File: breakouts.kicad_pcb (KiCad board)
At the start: 2 copper layers, 100 x 92.6 mm, 211 parts, among them IC901 ATTINY85-S, J1101 USB_MINI-B, J1201 JACK_5P, J201 USB_MINI-B, J301 USB_MINI-B, J401 SMA, J801 USB_MINI-B, K1201 CONN_3, K1301 CONN_3, K601 CONN_3, K801 CONN_3, P1001 CONN_4, P1002 CONN_4, P1101 CONN_6, P1102 CONN_6, P1201 CONN_2, P1202 CONN_2, P1203 CONN_2, P1301 CONN_2, P201 CONN_2, P202 CONN_2, P203 CONN_2, P301 CONN_6, P302 CONN_6, P401 CONN_8, P402 CONN_8, P501 CONN_2, P502 CONN_2, P701 POWER, P702 PORT B, P703 PORT C, P704 PORT D, P705 ISP, P801 PORT B, P802 PORT C, P803 PORT D, P804 ISP, P901 CONN_8, P902 ISP, SW701 SW_PUSH, SW801 SW_PUSH, SW901 SW_PUSH, U1001 SST25VF016B, U1101 FT230X-QFN, U1201 TDA1517ATW, U1301 MCP7940M, U301 FT230X, U401 MRF49XA, U501 SP6641A/B, U601 NX1117C33Z, U701 ATMEGA88PA-A, U801 ATMEGA32U2, X1301 32.768kHz, X401 10MHz, X701 12MHz 18pF, X801 16MHz 18pF

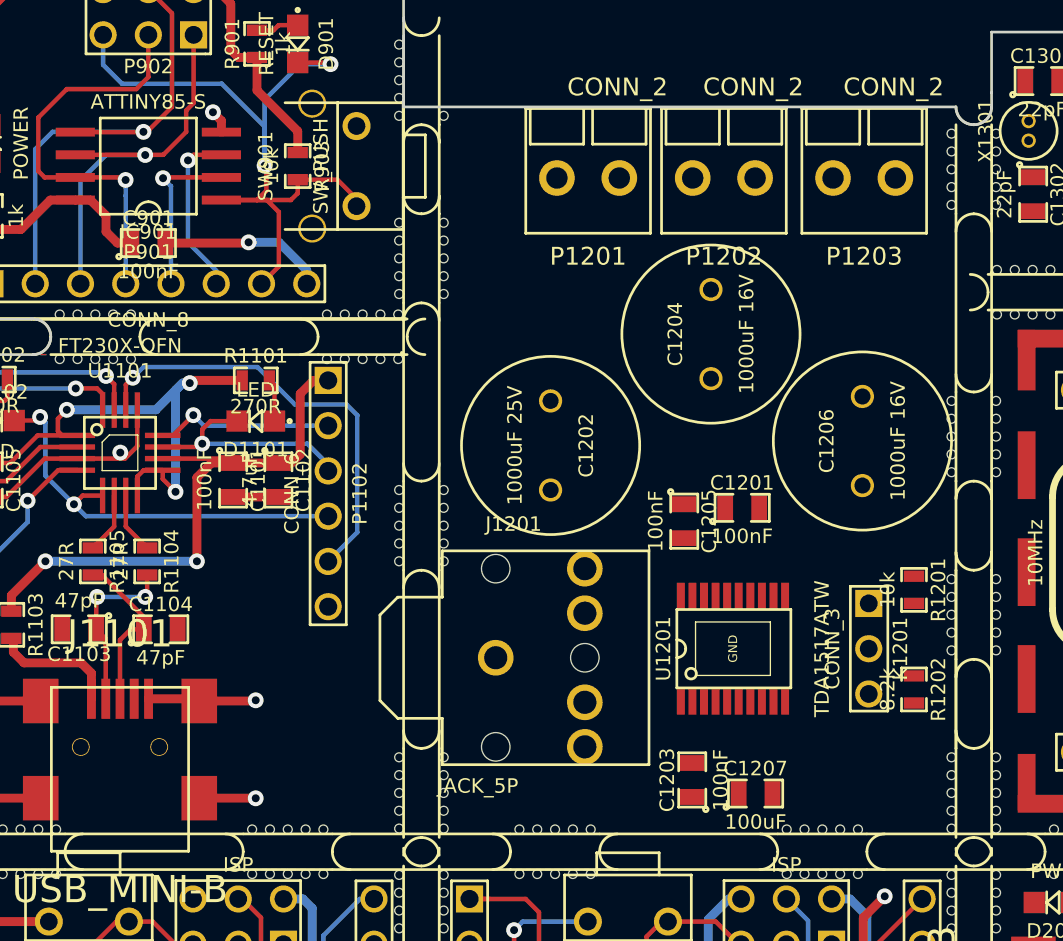
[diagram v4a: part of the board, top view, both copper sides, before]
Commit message: Route Audio amplifier board
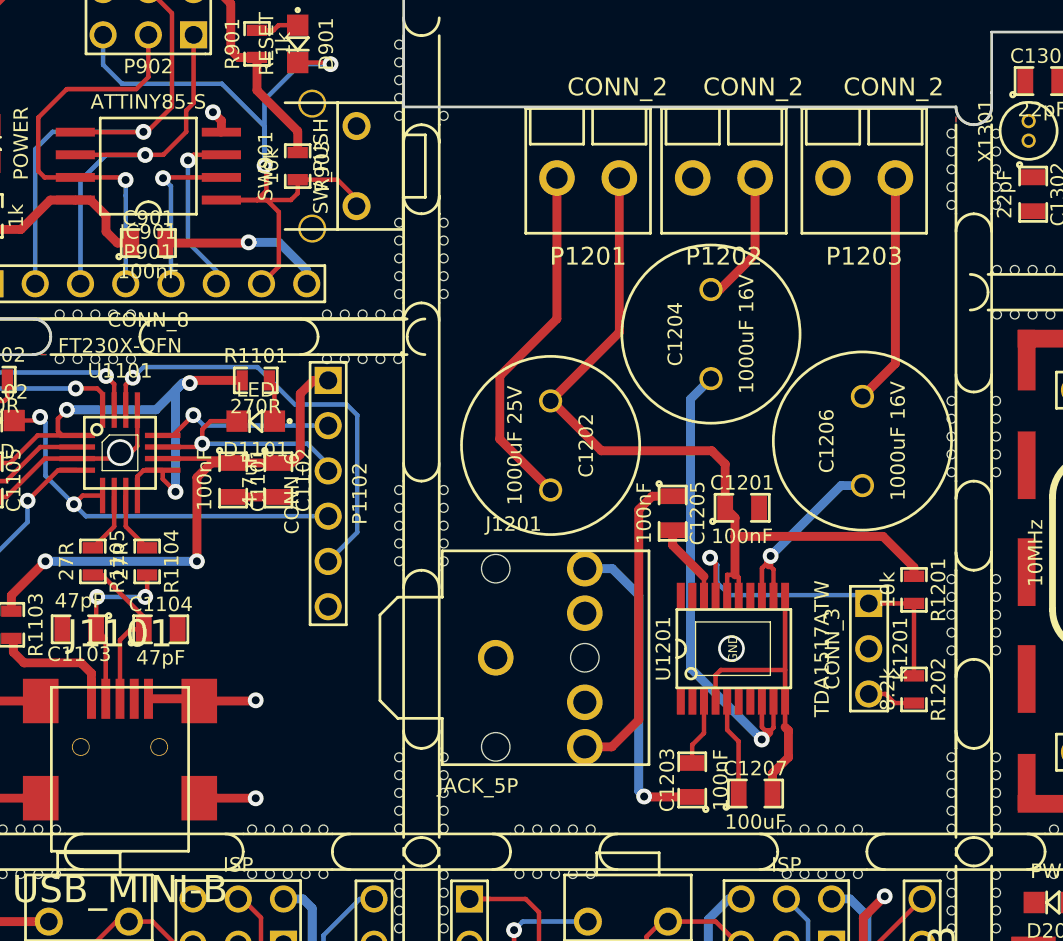
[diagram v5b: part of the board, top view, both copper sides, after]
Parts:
- moved C1205 0.79 mm to (70.1, 86.3)
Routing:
- net VCC11: track 0.00 -> 46.0 mm
- net GND11: track 0.00 -> 37.0 mm
- net N-00000168: track 0.00 -> 27.0 mm, vias 0 -> 1
- net /Audio amplifier/StandBy: track 0.00 -> 19.4 mm, vias 0 -> 1
- net N-00000161: track 0.00 -> 17.8 mm, vias 0 -> 1
- net N-00000162: track 0.00 -> 17.7 mm
- net N-00000170: track 0.00 -> 13.0 mm
- net N-00000166: track 0.00 -> 11.3 mm, vias 0 -> 1
- net N-00000169: track 0.00 -> 7.58 mm
- net N-00000158: track 0.00 -> 5.44 mm
- net N-00000160: track 0.00 -> 4.43 mm
- net N-00000159: track 0.00 -> 3.74 mm
- net /Audio amplifier/Mute: track 0.00 -> 2.75 mm
- net (no net): vias 2 -> 3
- added copper zone on B.Cu, net GND11
- added copper zone on F.Cu, net GND11

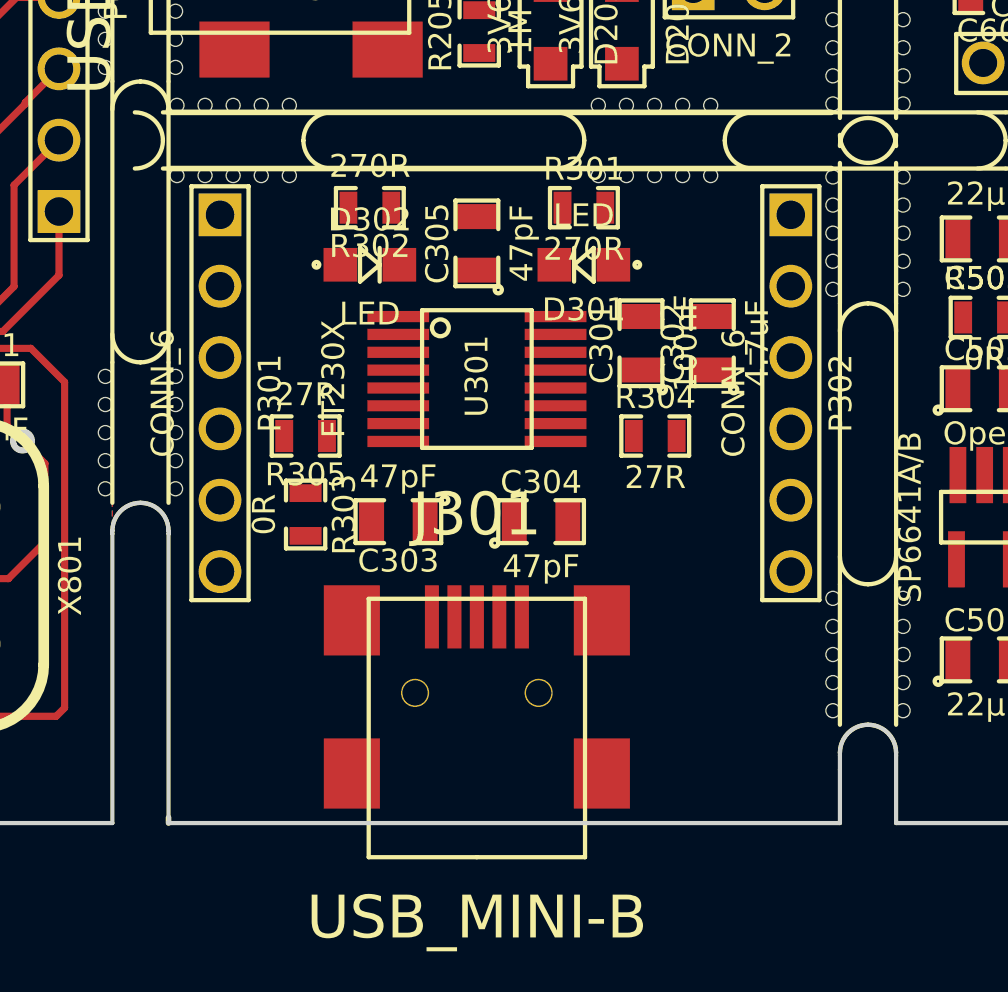
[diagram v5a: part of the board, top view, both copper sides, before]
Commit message: Route FT230X board
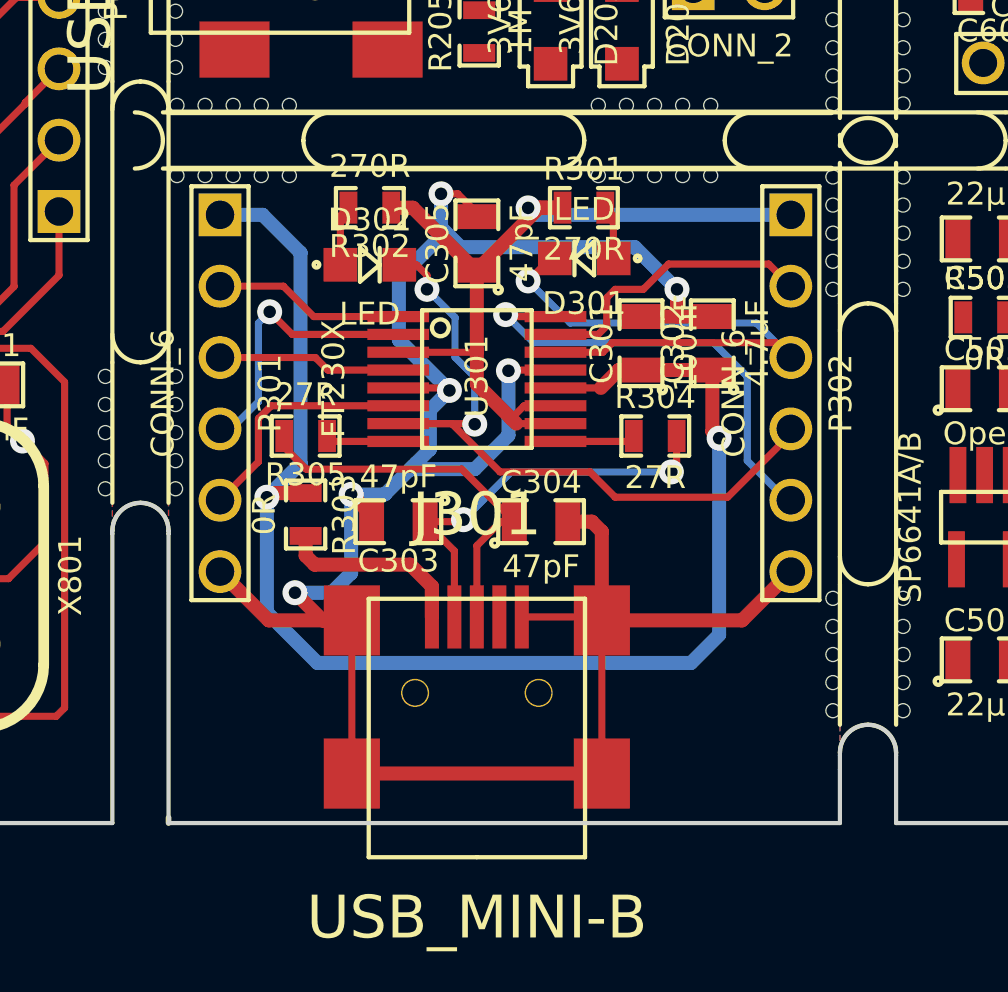
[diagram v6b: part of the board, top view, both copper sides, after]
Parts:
- moved D301 0.23 mm to (102.8, 127.4)
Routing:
- net GND2: track 0.00 -> 87.8 mm, vias 0 -> 6
- net VCC2: track 0.00 -> 50.8 mm, vias 0 -> 2
- net /FT230X/VCCIO: track 0.00 -> 30.8 mm, vias 0 -> 1
- net /FT230X/CBUS2: track 0.00 -> 26.1 mm, vias 0 -> 2
- net /FT230X/CBUS1: track 0.00 -> 20.5 mm, vias 0 -> 1
- net /FT230X/CBUS3: track 0.00 -> 16.5 mm, vias 0 -> 1
- net N-0000022: track 0.00 -> 14.7 mm, vias 0 -> 2
- net N-0000023: track 0.00 -> 13.9 mm
- net /FT230X/CBUS0: track 0.00 -> 10.3 mm
- net /FT230X/~RTS: track 0.00 -> 10.0 mm, vias 0 -> 1
- net /FT230X/~CTS: track 0.00 -> 8.64 mm
- net /FT230X/TxD: track 0.00 -> 6.79 mm
- net N-0000021: track 0.00 -> 6.74 mm
- net /FT230X/RxD: track 0.00 -> 6.53 mm
- net N-0000018: track 0.00 -> 2.87 mm
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- added copper zone on B.Cu, net GND2
- added copper zone on F.Cu, net GND2

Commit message: Route step-up and voltage regulator boards
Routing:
- net GND5: track 0.00 -> 17.4 mm, vias 0 -> 2
- net /step-up/VBATT: track 0.00 -> 17.0 mm
- net GND4: track 0.00 -> 15.4 mm, vias 0 -> 1
- net /voltage-reg/Vout: track 0.00 -> 13.2 mm
- net N-0000046: track 0.00 -> 9.83 mm
- net /step-up/Vout: track 0.00 -> 9.13 mm
- net /voltage-reg/Vin: track 0.00 -> 6.72 mm
- net N-0000049: track 0.00 -> 5.69 mm
- added copper zone on B.Cu, net GND4
- added copper zone on F.Cu, net GND4
- added copper zone on B.Cu, net GND5
- added copper zone on F.Cu, net GND5
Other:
- outline, holes or cut-outs redrawn

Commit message: Route Flash and RTC boards
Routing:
- net GND1: track 0.00 -> 41.0 mm
- net VCC1: track 0.00 -> 25.8 mm, vias 0 -> 1
- net VCC12: track 0.00 -> 22.3 mm
- net N-000001: track 0.00 -> 21.1 mm, vias 0 -> 2
- net GND12: track 0.00 -> 19.0 mm
- net N-000002: track 0.00 -> 18.2 mm
- net GND9: track 0.00 -> 11.3 mm
- net VCC9: track 0.00 -> 9.44 mm
- net N-00000183: track 0.00 -> 8.66 mm
- net N-00000186: track 0.00 -> 8.57 mm
- net N-00000185: track 0.00 -> 6.99 mm
- net N-00000179: track 0.00 -> 5.50 mm
- net N-00000180: track 0.00 -> 5.34 mm
- net N-00000134: track 0.00 -> 4.83 mm
- net N-00000131: track 0.00 -> 3.19 mm
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- added copper zone on B.Cu, net GND1
- added copper zone on F.Cu, net GND1
- added copper zone on B.Cu, net GND12
- added copper zone on F.Cu, net GND12
- added copper zone on B.Cu, net GND9
- added copper zone on F.Cu, net GND9
